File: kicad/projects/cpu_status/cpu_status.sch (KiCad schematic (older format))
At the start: 103 parts, among them J1 Control_signal_backplane, J2 Aux_connection, J3 Bus_connection, J4 MAR_content_in, U1 74HC245, U2 74HC245, U3 74HC245, U4 74HC245, U5 74HC245, U6 74HC245, U7 74HC245, U8 74HC245, U9 74HC126

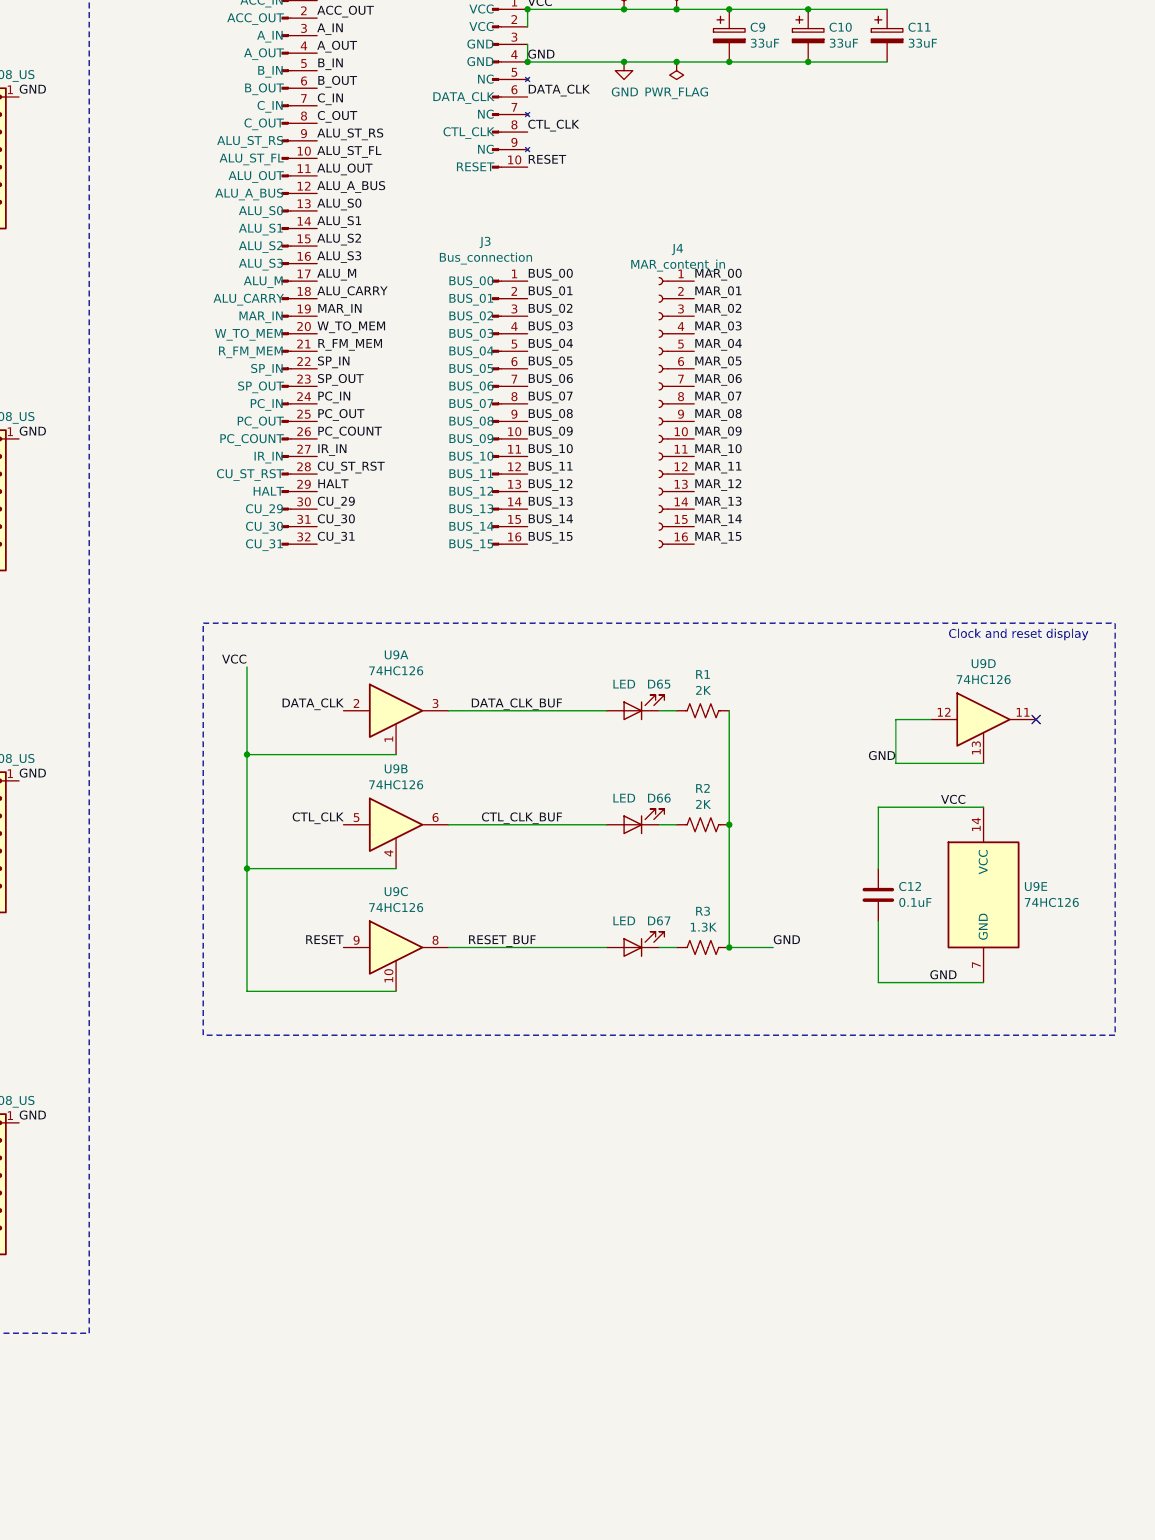
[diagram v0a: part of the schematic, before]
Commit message: Added power port and LED control to status board.
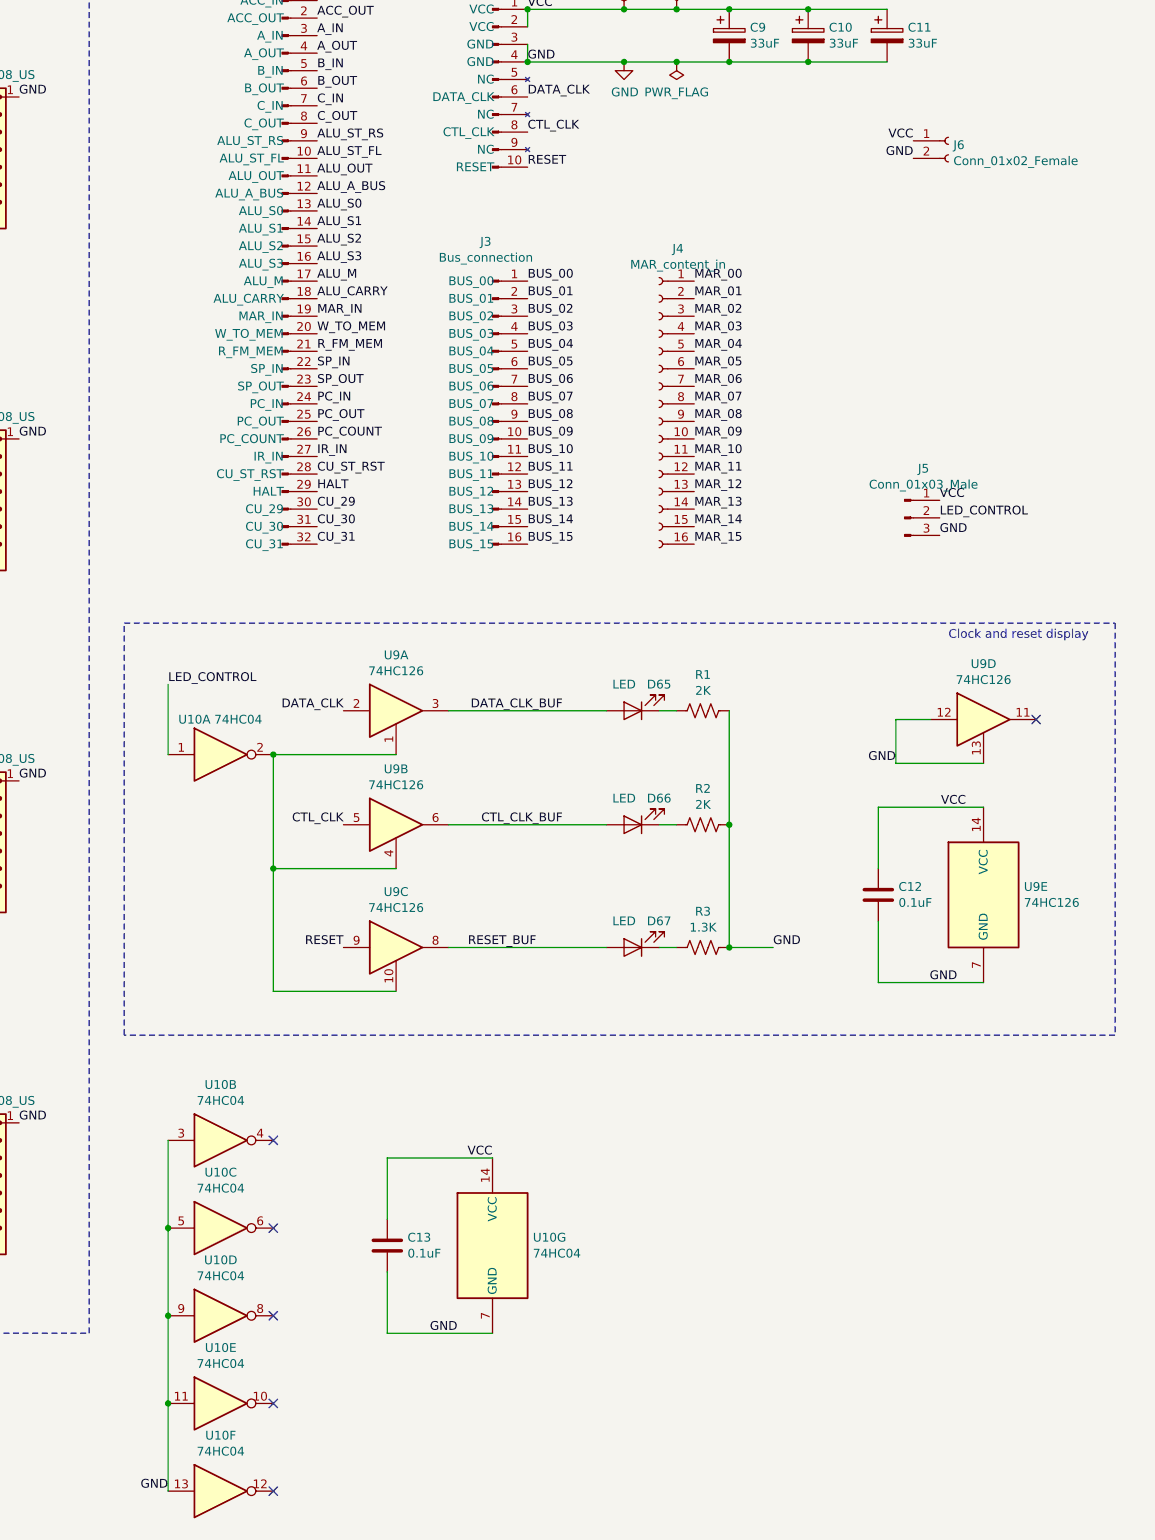
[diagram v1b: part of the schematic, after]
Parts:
- added C13: 0.1uF, Capacitor_THT:C_Disc_D4.7mm_W2.5mm_P5.00mm, symbol Device:C
- added J5: Conn_01x03_Male, Connector_PinHeader_2.54mm:PinHeader_1x03_P2.54mm_Horizontal, symbol Connector:Conn_01x03_Male
- added J6: Conn_01x02_Female, Connector_PinSocket_2.54mm:PinSocket_1x02_P2.54mm_Horizontal, symbol Connector:Conn_01x02_Female
- added U10: 74HC04, Package_DIP:DIP-14_W7.62mm, symbol 74xx:74HC04
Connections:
- net GND: now also C13.2, J5.3 (Pin_3), J6.2 (Pin_2), U10.11, U10.13, U10.3, U10.5, U10.7 (GND), U10.9
- net VCC: now also C13.1, J5.1 (Pin_1), J6.1 (Pin_1), U10.14 (VCC); no longer U9.1, U9.10, U9.4
- new net: U10.2, U9.1, U9.10, U9.4
- new net LED_CONTROL: J5.2 (Pin_2), U10.1
- no-connect marks 1 -> 6
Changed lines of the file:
@@
 Wire Wire Line
 	14900 5700 14400 5700
-Text Label 10700 5150 2    50   ~ 0
-VCC
 Text Label 13700 6750 0    50   ~ 0
 GND
 Wire Wire Line
-	10700 5150 10700 5650
-Wire Wire Line
-	10700 5650 11550 5650
-Wire Wire Line
-	10700 5650 10700 6300
-Wire Wire Line
-	10700 6300 11550 6300
-Connection ~ 10700 5650
-Wire Wire Line
-	10700 6300 10700 7000
-Wire Wire Line
-	10700 7000 11550 7000
-Connection ~ 10700 6300
+	10850 5650 11550 5650
+Wire Wire Line
+	10850 5650 10850 6300
+Wire Wire Line
+	10850 6300 11550 6300
+Connection ~ 10850 5650
+Wire Wire Line
+	10850 6300 10850 7000
+Wire Wire Line
+	10850 7000 11550 7000
+Connection ~ 10850 6300
 Wire Wire Line
 	13700 6750 13450 6750
@@
 	11850 6750 12750 6750
 Wire Notes Line
-	10450 4900 15650 4900
+	10000 4900 15650 4900
 Wire Notes Line
 	15650 4900 15650 7250
 Wire Notes Line
-	15650 7250 10450 7250
-Wire Notes Line
-	10450 7250 10450 4900
+	15650 7250 10000 7250
+Wire Notes Line
+	10000 7250 10000 4900
 Text Notes 14700 5000 0    50   ~ 0
 Clock and reset display
+$Comp
+L Connector:Conn_01x02_Female J6
+U 1 1 63B97B5B
+P 14700 2150
+F 0 "J6" H 14728 2126 50  0000 L CNN
+F 1 "Conn_01x02_Female" H 14728 2035 50  0000 L CNN
+F 2 "Connector_PinSocket_2.54mm:PinSocket_1x02_P2.54mm_Horizontal" H 14700 2150 50  0001 C CNN
+F 3 "~" H 14700 2150 50  0001 C CNN
+	1    14700 2150
+	1    0    0    -1
+$EndComp
+$Comp
+L Connector:Conn_01x03_Male J5
+U 1 1 63B98030
+P 14450 4300
+F 0 "J5" H 14558 4581 50  0000 C CNN
+F 1 "Conn_01x03_Male" H 14558 4490 50  0000 C CNN
+F 2 "Connector_PinHeader_2.54mm:PinHeader_1x03_P2.54mm_Horizontal" H 14450 4300 50  0001 C CNN
+F 3 "~" H 14450 4300 50  0001 C CNN
+	1    14450 4300
+	1    0    0    -1
+$EndComp
+Text Label 14650 4300 0    50   ~ 0
+LED_CONTROL
+Text Label 14650 4200 0    50   ~ 0
+VCC
+Text Label 14650 4400 0    50   ~ 0
+GND
+Text Label 14500 2150 2    50   ~ 0
+VCC
+Text Label 14500 2250 2    50   ~ 0
+GND
+$Comp
+L 74xx:74HC04 U10
+U 1 1 63BE26BD
+P 10550 5650
+F 0 "U10" H 10400 5850 50  0000 C CNN
+F 1 "74HC04" H 10650 5850 50  0000 C CNN
+F 2 "Package_DIP:DIP-14_W7.62mm" H 10550 5650 50  0001 C CNN
+F 3 "https://assets.nexperia.com/documents/data-sheet/74HC_HCT04.pdf" H 10550 5650 50  0001 C CNN
+	1    10550 5650
+	1    0    0    -1
+$EndComp
+$Comp
+L 74xx:74HC04 U10
+U 2 1 63BE45A0
+P 10550 7850
+F 0 "U10" H 10550 8167 50  0000 C CNN
+F 1 "74HC04" H 10550 8076 50  0000 C CNN
+F 2 "Package_DIP:DIP-14_W7.62mm" H 10550 7850 50  0001 C CNN
+F 3 "https://assets.nexperia.com/documents/data-sheet/74HC_HCT04.pdf" H 10550 7850 50  0001 C CNN
+	2    10550 7850
+	1    0    0    -1
+$EndComp
+$Comp
+L 74xx:74HC04 U10
+U 3 1 63BE63FC
+P 10550 8350
+F 0 "U10" H 10550 8667 50  0000 C CNN
+F 1 "74HC04" H 10550 8576 50  0000 C CNN
+F 2 "Package_DIP:DIP-14_W7.62mm" H 10550 8350 50  0001 C CNN
+F 3 "https://assets.nexperia.com/documents/data-sheet/74HC_HCT04.pdf" H 10550 8350 50  0001 C CNN
+	3    10550 8350
+	1    0    0    -1
+$EndComp
+$Comp
+L 74xx:74HC04 U10
+U 4 1 63BE8569
+P 10550 8850
+F 0 "U10" H 10550 9167 50  0000 C CNN
+F 1 "74HC04" H 10550 9076 50  0000 C CNN
+F 2 "Package_DIP:DIP-14_W7.62mm" H 10550 8850 50  0001 C CNN
+F 3 "https://assets.nexperia.com/documents/data-sheet/74HC_HCT04.pdf" H 10550 8850 50  0001 C CNN
+	4    10550 8850
+	1    0    0    -1
+$EndComp
+$Comp
+L 74xx:74HC04 U10
+U 5 1 63BE9611
+P 10550 9350
+F 0 "U10" H 10550 9667 50  0000 C CNN
+F 1 "74HC04" H 10550 9576 50  0000 C CNN
+F 2 "Package_DIP:DIP-14_W7.62mm" H 10550 9350 50  0001 C CNN
+F 3 "https://assets.nexperia.com/documents/data-sheet/74HC_HCT04.pdf" H 10550 9350 50  0001 C CNN
+	5    10550 9350
+	1    0    0    -1
+$EndComp
+$Comp
+L 74xx:74HC04 U10
+U 6 1 63BEC45B
+P 10550 9850
+F 0 "U10" H 10550 10167 50  0000 C CNN
+F 1 "74HC04" H 10550 10076 50  0000 C CNN
+F 2 "Package_DIP:DIP-14_W7.62mm" H 10550 9850 50  0001 C CNN
+F 3 "https://assets.nexperia.com/documents/data-sheet/74HC_HCT04.pdf" H 10550 9850 50  0001 C CNN
+	6    10550 9850
+	1    0    0    -1
+$EndComp
+$Comp
+L 74xx:74HC04 U10
+U 7 1 63BEF1BC
+P 12100 8450
+F 0 "U10" H 12330 8496 50  0000 L CNN
+F 1 "74HC04" H 12330 8405 50  0000 L CNN
+F 2 "Package_DIP:DIP-14_W7.62mm" H 12100 8450 50  0001 C CNN
+F 3 "https://assets.nexperia.com/documents/data-sheet/74HC_HCT04.pdf" H 12100 8450 50  0001 C CNN
+	7    12100 8450
+	1    0    0    -1
+$EndComp
+Text Label 10250 5250 0    50   ~ 0
+LED_CONTROL
+Wire Wire Line
+	10250 5650 10250 5250
+$Comp
+L Device:C C13
+U 1 1 63DC8749
+P 11500 8450
+F 0 "C13" H 11615 8496 50  0000 L CNN
+F 1 "0.1uF" H 11615 8405 50  0000 L CNN
+F 2 "Capacitor_THT:C_Disc_D4.7mm_W2.5mm_P5.00mm" H 11538 8300 50  0001 C CNN
+F 3 "~" H 11500 8450 50  0001 C CNN
+	1    11500 8450
+	1    0    0    -1
+$EndComp
+Wire Wire Line
+	12100 7950 11500 7950
+Wire Wire Line
+	11500 7950 11500 8300
+Wire Wire Line
+	11500 8600 11500 8950
+Wire Wire Line
+	11500 8950 12100 8950
+Text Label 12100 7950 2    50   ~ 0
+VCC
+Text Label 11900 8950 2    50   ~ 0
+GND
+NoConn ~ 10850 7850
+NoConn ~ 10850 8350
+NoConn ~ 10850 8850
+NoConn ~ 10850 9350
+NoConn ~ 10850 9850
+Wire Wire Line
+	10250 7850 10250 8350
+Connection ~ 10250 8350
+Wire Wire Line
+	10250 8350 10250 8850
+Connection ~ 10250 8850
+Wire Wire Line
+	10250 8850 10250 9350
+Connection ~ 10250 9350
+Wire Wire Line
+	10250 9350 10250 9850
+Text Label 10250 9850 2    50   ~ 0
+GND
 $EndSCHEMATC

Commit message: Finish wiring on CPU Status.
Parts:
- added R4: 10K, Resistor_THT:R_Axial_DIN0207_L6.3mm_D2.5mm_P10.16mm_Horizontal, symbol Device:R_US
- D1, D10, D11, D12, D13, D14, D15, D16, D17, D18, D19, D2, D20, D21, D22, D23, D24, D25, D26, D27, D28, D29, D3, D30, D31, D32, D33, D34, D35, D36, D37, D38, D39, D4, D40, D41, D42, D43, D44, D45, D46, D47, D48, D49, D5, D50, D51, D52, D53, D54, D55, D56, D57, D58, D59, D6, D60, D61, D62, D63, D64, D65, D66, D67, D7, D8, D9: footprint LED_THT:LED_D5.0mm -> sixteen-bit-computer:LED_D5.0mm
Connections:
- net GND: now also R4.1; no longer U1.19 (~OE), U2.19 (~OE), U3.19 (~OE), U4.19 (~OE), U5.19 (~OE), U6.19 (~OE), U7.19 (~OE), U8.19 (~OE)
- net LED_CONTROL: now also U1.19 (~OE), U2.19 (~OE), U3.19 (~OE), U4.19 (~OE), U5.19 (~OE), U6.19 (~OE), U7.19 (~OE), U8.19 (~OE), R4.2
